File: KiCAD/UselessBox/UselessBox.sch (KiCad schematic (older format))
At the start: 13 parts, among them J1 Power IN, J2 Switch (2 x On), J4 Servo Door, J5 Servo Finger, J6 Calibration Switches, K1 G5V-2, Q1 BC107

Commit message: PCB completed
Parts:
- A1: symbol MCU_Module:Arduino_Nano_v3.x -> UselessBox-rescue:Arduino_Nano_v3.x-MCU_Module
- C1: footprint Capacitor_THT:CP_Radial_D12.5mm_P5.00mm -> Capacitor_THT:CP_Radial_D8.0mm_P5.00mm
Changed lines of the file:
@@
 EESchema Schematic File Version 4
-LIBS:UselessBox-cache
-EELAYER 26 0
+EELAYER 30 0
 EELAYER END
 $Descr A4 11693 8268
@@
 $EndDescr
 $Comp
-L MCU_Module:Arduino_Nano_v3.x A1
+L UselessBox-rescue:Arduino_Nano_v3.x-MCU_Module A1
 U 1 1 5FD0EDD7
 P 3950 3500
@@
 F 0 "C1" H 5550 2550 50  0000 L CNN
 F 1 "CP" H 5568 2455 50  0000 L CNN
-F 2 "Capacitor_THT:CP_Radial_D12.5mm_P5.00mm" H 5488 2350 50  0001 C CNN
+F 2 "Capacitor_THT:CP_Radial_D8.0mm_P5.00mm" H 5488 2350 50  0001 C CNN
 F 3 "~" H 5450 2500 50  0001 C CNN
 	1    5450 2500

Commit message: Double check and minor fixes
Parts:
- C1: value CP -> 100 uF; footprint Capacitor_THT:CP_Radial_D8.0mm_P5.00mm -> Capacitor_THT:CP_Radial_D6.3mm_P2.50mm
- R1, R2: value R -> 10k
- R3: value R -> 47k
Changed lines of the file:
@@
 P 5450 2500
 F 0 "C1" H 5550 2550 50  0000 L CNN
-F 1 "CP" H 5568 2455 50  0000 L CNN
-F 2 "Capacitor_THT:CP_Radial_D8.0mm_P5.00mm" H 5488 2350 50  0001 C CNN
+F 1 "100 uF" H 5568 2455 50  0000 L CNN
+F 2 "Capacitor_THT:CP_Radial_D6.3mm_P2.50mm" H 5488 2350 50  0001 C CNN
 F 3 "~" H 5450 2500 50  0001 C CNN
 	1    5450 2500
@@
 P 5100 3250
 F 0 "R1" H 5170 3296 50  0000 L CNN
-F 1 "R" H 5170 3205 50  0000 L CNN
+F 1 "10k" H 5170 3205 50  0000 L CNN
 F 2 "Resistor_THT:R_Axial_DIN0204_L3.6mm_D1.6mm_P7.62mm_Horizontal" V 5030 3250 50  0001 C CNN
 F 3 "~" H 5100 3250 50  0001 C CNN
@@
 P 5100 3750
 F 0 "R2" H 5170 3796 50  0000 L CNN
-F 1 "R" H 5170 3705 50  0000 L CNN
+F 1 "10k" H 5170 3705 50  0000 L CNN
 F 2 "Resistor_THT:R_Axial_DIN0204_L3.6mm_D1.6mm_P7.62mm_Horizontal" V 5030 3750 50  0001 C CNN
 F 3 "~" H 5100 3750 50  0001 C CNN
@@
 P 1950 4250
 F 0 "R3" H 2020 4296 50  0000 L CNN
-F 1 "R" H 2020 4205 50  0000 L CNN
+F 1 "47k" H 2020 4205 50  0000 L CNN
 F 2 "Resistor_THT:R_Axial_DIN0204_L3.6mm_D1.6mm_P7.62mm_Horizontal" V 1880 4250 50  0001 C CNN
 F 3 "~" H 1950 4250 50  0001 C CNN

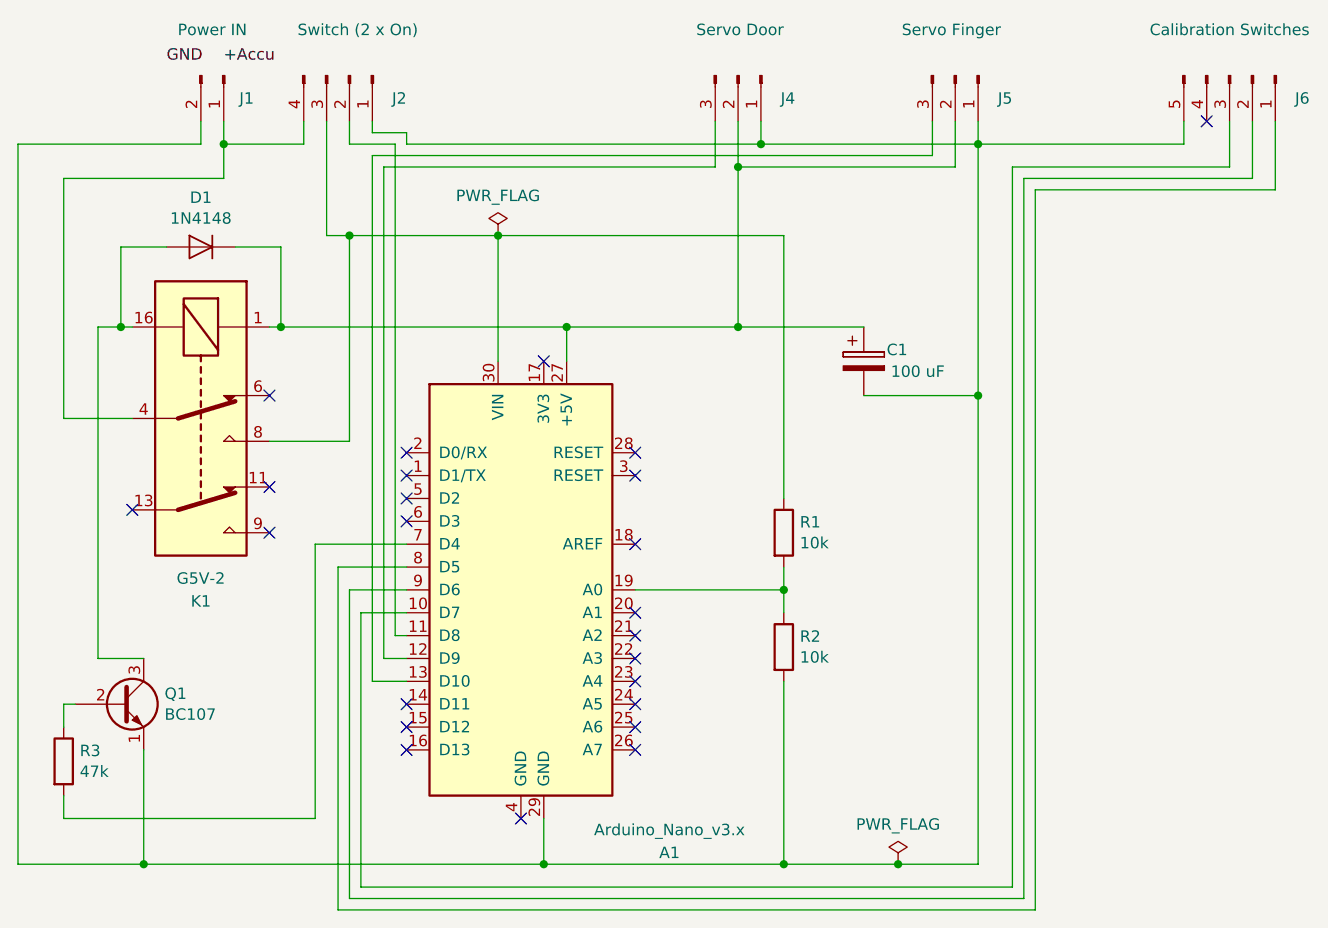
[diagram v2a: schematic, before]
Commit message: Sanitize servo positions. Add PCB images and schema PDF
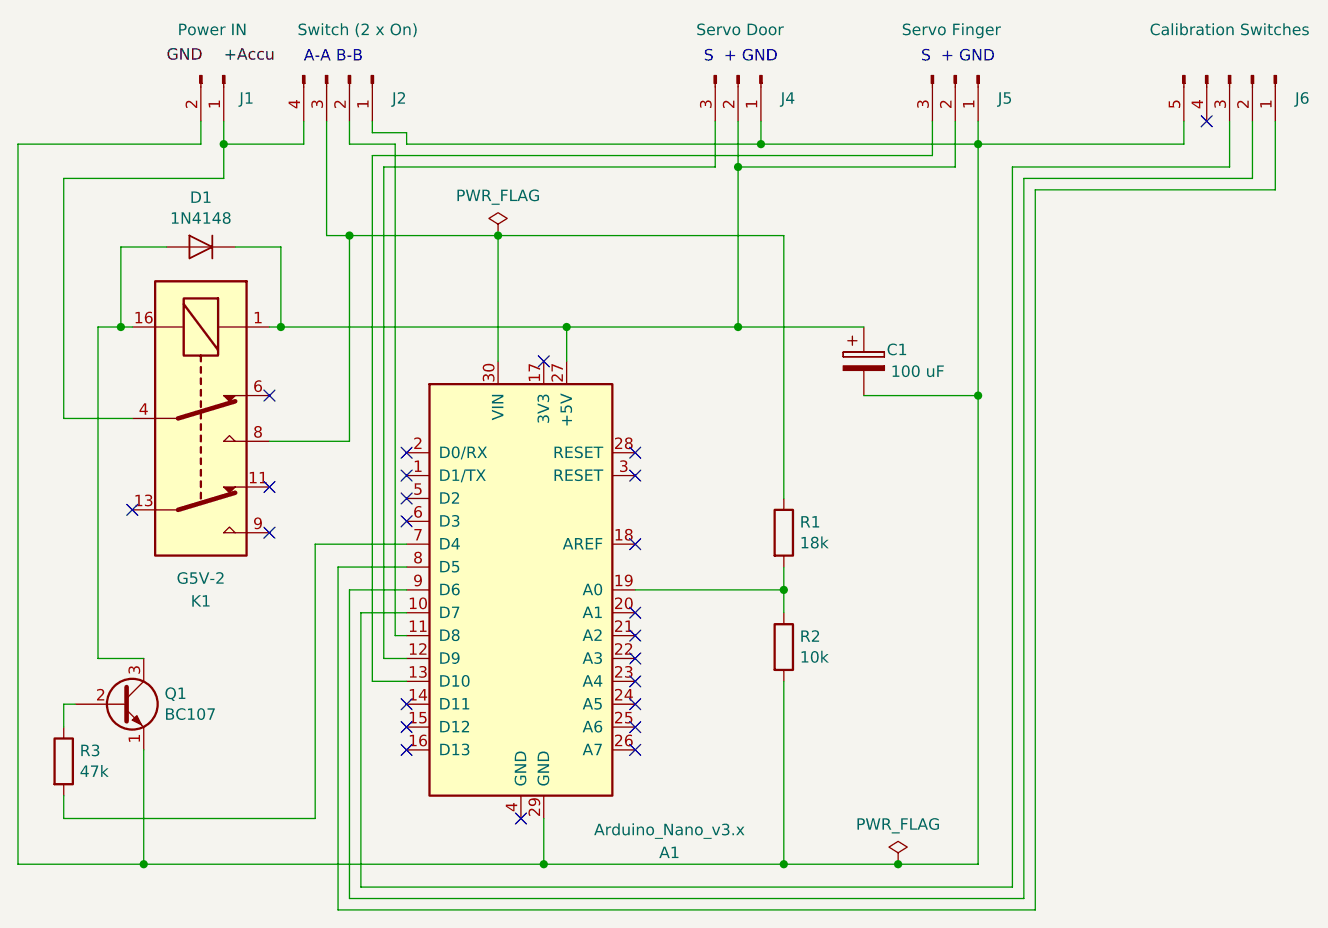
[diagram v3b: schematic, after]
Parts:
- R1: value 10k -> 18k
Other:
- note added: "A-A B-B"
- note added: "S + GND"
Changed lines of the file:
@@
 EESchema Schematic File Version 4
-EELAYER 30 0
+LIBS:UselessBox-cache
+EELAYER 26 0
 EELAYER END
 $Descr A4 11693 8268
@@
 P 5100 3250
 F 0 "R1" H 5170 3296 50  0000 L CNN
-F 1 "10k" H 5170 3205 50  0000 L CNN
+F 1 "18k" H 5170 3205 50  0000 L CNN
 F 2 "Resistor_THT:R_Axial_DIN0204_L3.6mm_D1.6mm_P7.62mm_Horizontal" V 5030 3250 50  0001 C CNN
 F 3 "~" H 5100 3250 50  0001 C CNN
@@
 Wire Wire Line
 	3450 1550 5000 1550
+Text Notes 3000 1200 0    50   ~ 0
+A-A B-B
+Text Notes 4750 1200 0    50   ~ 0
+S  + GND
+Text Notes 5700 1200 0    50   ~ 0
+S  + GND
 $EndSCHEMATC
